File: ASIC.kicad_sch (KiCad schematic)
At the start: 122 parts, among them U13 TS3011, U14 SN74AVC2T45DCUR, U15 25MHz, U16 TLV75512PDQNR, U17 TLV755075PDQNR, U18 TLV75512PDQNR, U3 TLV755075PDQNR, U8 25MHz

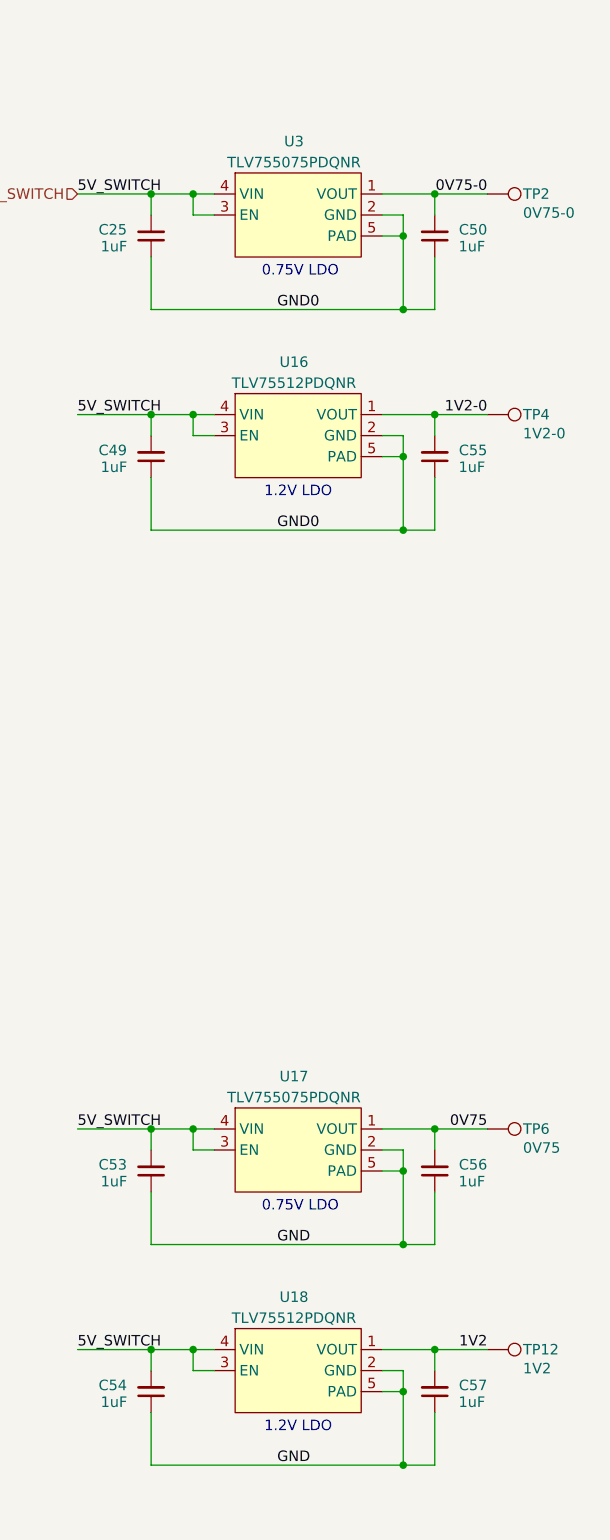
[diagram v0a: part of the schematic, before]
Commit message: switched to larger LDOs. 0.75V -> 0.8V. Tweaked power planes some more
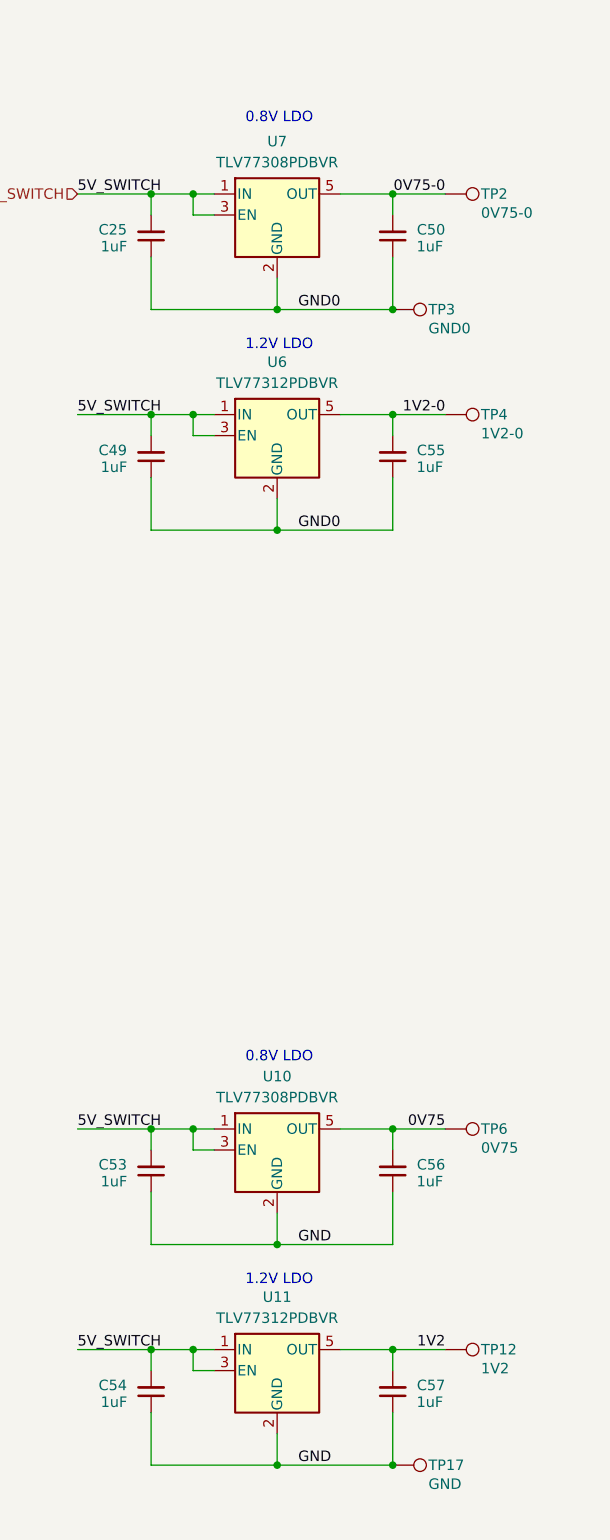
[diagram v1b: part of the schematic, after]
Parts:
- removed U16, U18: TLV75512PDQNR, bitaxe:DQN0004A, symbol bitaxe:TLV755P
- removed U17, U3: TLV755075PDQNR, bitaxe:DQN0004A, symbol bitaxe:TLV755P
- added TP17: GND, bitaxe:TestPoint_Pad_D1.0mm, symbol Connector:TestPoint
- added TP3: GND0, bitaxe:TestPoint_Pad_D1.0mm, symbol Connector:TestPoint
- added U10, U7: TLV77308PDBVR, Package_TO_SOT_SMD:SOT-23-5, symbol Regulator_Linear:TLV73312PDBV
- added U11, U6: TLV77312PDBVR, Package_TO_SOT_SMD:SOT-23-5, symbol Regulator_Linear:TLV73312PDBV
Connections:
- net 0V75: now also U10.5 (OUT)
- net 0V75-0: now also U7.5 (OUT)
- net 1V2: now also U11.5 (OUT)
- net 1V2-0: now also U6.5 (OUT)
- net 5V_SWITCH: now also U10.1 (IN), U10.3 (EN), U11.1 (IN), U11.3 (EN), U6.1 (IN), U6.3 (EN), U7.1 (IN), U7.3 (EN)
- net GND: now also TP17.1, U10.2 (GND), U11.2 (GND)
- net GND0: now also TP3.1, U6.2 (GND), U7.2 (GND)
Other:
- note added: "0.8V LDO"
- note removed: "0.75V LDO"
- moved on the sheet: C50, C55, C56, C57, TP12, TP2, TP4, TP6
